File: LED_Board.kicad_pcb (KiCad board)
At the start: 2 copper layers, 84.2 x 88.2 mm, 26 parts, among them J1 Conn_01x06, J2 Conn_01x02, SW1 SW_Push, U1 PCA9531PW_LED_Driver_i2c

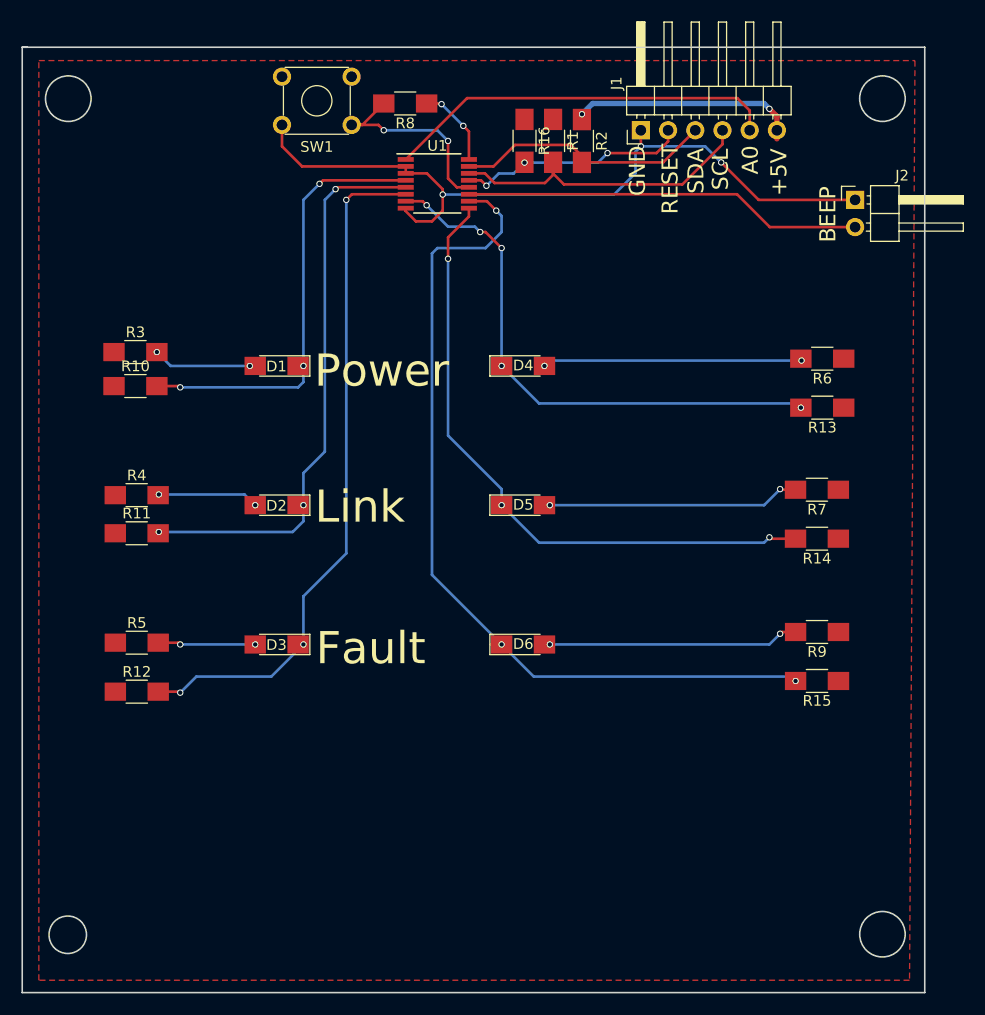
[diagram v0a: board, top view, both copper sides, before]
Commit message: Arduino code able to read/write
Fixed a bug that stopped the code reading the status of the input pins.

Updated the PCB files based on the findings that I made during bring-up.
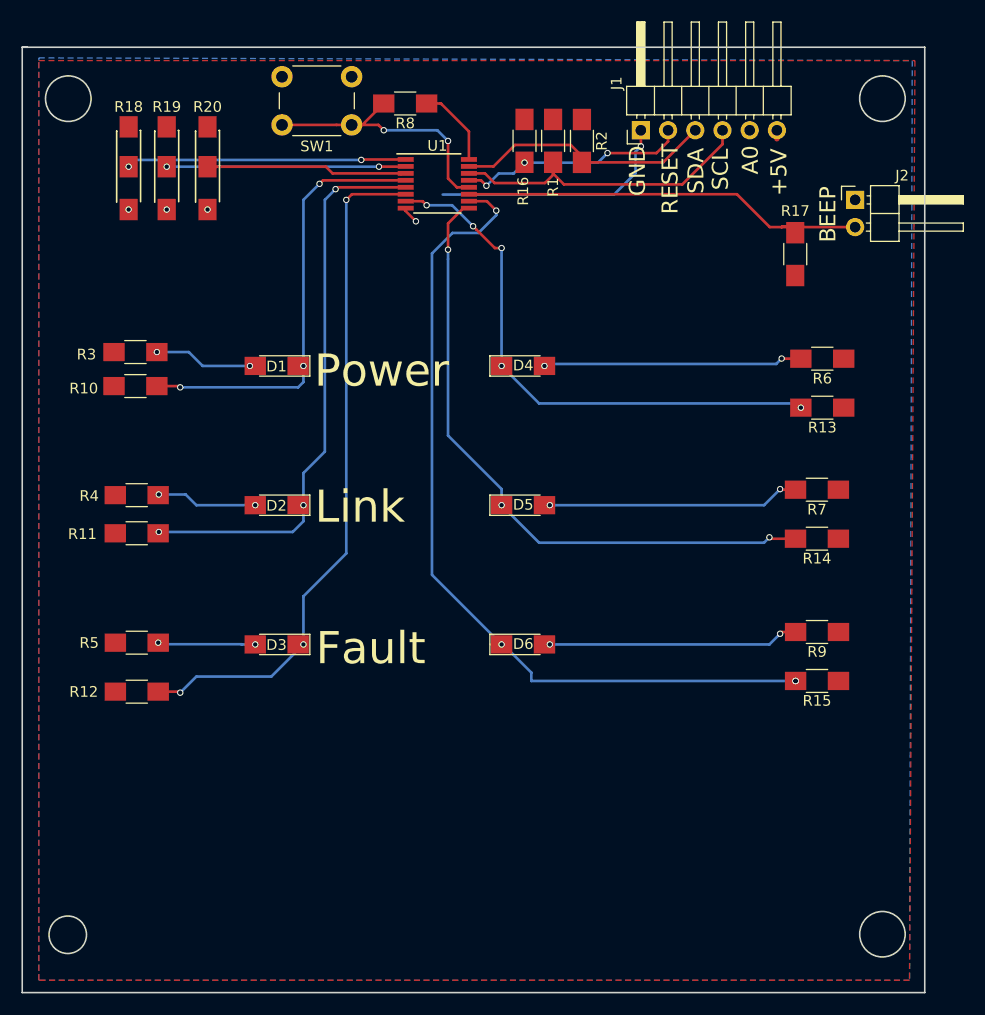
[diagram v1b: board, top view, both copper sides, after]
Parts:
- added R17: R, Resistors_SMD:R_1206_HandSoldering, F.Cu at (121.4, 49.6)
- added R18: R, TJS-Kicad:R_1206_Jumper, F.Cu at (59.2, 43.4)
- added R19: R, TJS-Kicad:R_1206_Jumper, F.Cu at (62.7, 43.4)
- added R20: R, TJS-Kicad:R_1206_Jumper, F.Cu at (66.5, 43.4)
- SW1: footprint Buttons_Switches_THT:SW_TH_Tactile_Omron_B3F-10xx -> Buttons_Switches_THT:SW_PUSH_6mm
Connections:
- J1 pad 5: /A0 -> Net-(J1-Pad5)
- J2 pad 1: GND -> VDD
- U1 pad 1: /A0 -> Net-(R18-Pad2)
- U1 pad 2: GND -> Net-(R19-Pad2)
- U1 pad 3: GND -> Net-(R20-Pad2)
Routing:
- net GND: track 70.7 -> 24.7 mm, vias 3 -> 5
- net /A0: track 36.8 -> 0.00 mm
- net Net-(R18-Pad2): track 0.00 -> 26.1 mm, vias 0 -> 2
- net Net-(R19-Pad2): track 0.00 -> 22.3 mm, vias 0 -> 2
- net VDD: track 30.4 -> 9.54 mm, vias 4 -> 0
- net Net-(R20-Pad2): track 0.00 -> 19.0 mm
- net /SWITCH: track 19.2 -> 25.7 mm
- net /BEEP: track 37.3 -> 38.9 mm
- net Net-(D6-Pad1): track 81.5 -> 80.3 mm, vias 3 -> 4
- added copper zone on B.Cu, net GND
